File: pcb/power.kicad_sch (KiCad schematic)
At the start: 29 parts

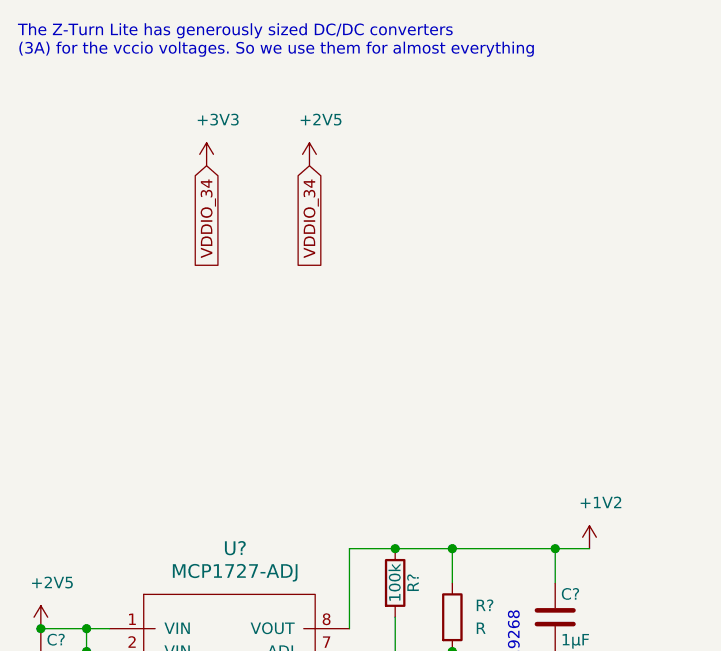
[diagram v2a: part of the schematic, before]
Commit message: add i2c addresses
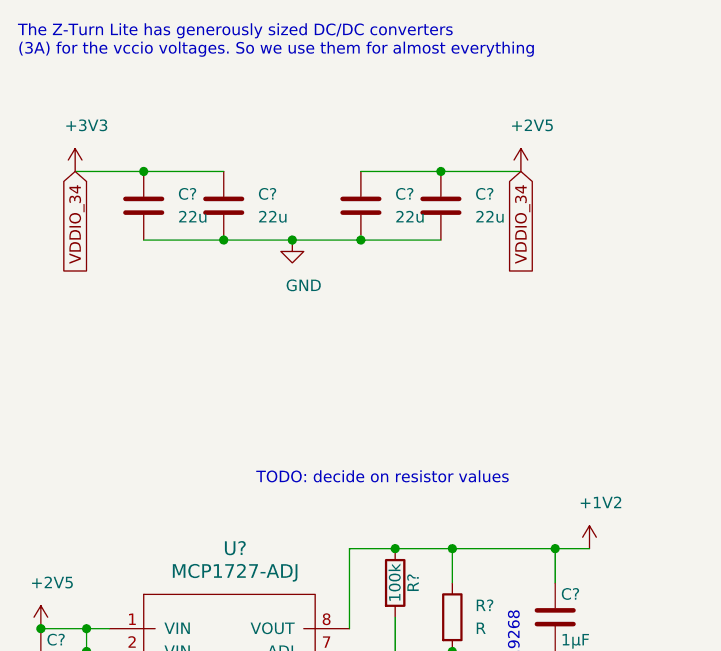
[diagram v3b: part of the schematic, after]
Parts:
- added C? (x4): 22u, symbol Device:C
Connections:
- net +2V5: now also C?.1, C?.1, C?.1, C?.1
- net GND: now also C?.2, C?.2, C?.2, C?.2
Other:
- note added: "TODO: decide on resistor values"
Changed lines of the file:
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@@
   (junction (at 36.83 163.83) (diameter 1.016) (color 0 0 0 0))
   (junction (at 36.83 166.37) (diameter 1.016) (color 0 0 0 0))
+  (junction (at 43.18 36.83) (diameter 1.016) (color 0 0 0 0))
+  (junction (at 52.07 44.45) (diameter 1.016) (color 0 0 0 0))
+  (junction (at 59.69 44.45) (diameter 1.016) (color 0 0 0 0))
+  (junction (at 67.31 44.45) (diameter 1.016) (color 0 0 0 0))
   (junction (at 71.12 78.74) (diameter 1.016) (color 0 0 0 0))
   (junction (at 71.12 115.57) (diameter 1.016) (color 0 0 0 0))
   (junction (at 71.12 154.94) (diameter 1.016) (color 0 0 0 0))
+  (junction (at 76.2 36.83) (diameter 1.016) (color 0 0 0 0))
   (junction (at 77.47 78.74) (diameter 1.016) (color 0 0 0 0))
   (junction (at 77.47 90.17) (diameter 1.016) (color 0 0 0 0))
@@
     (stroke (width 0) (type solid) (color 0 0 0 0))
   )
+  (wire (pts (xy 35.56 36.83) (xy 43.18 36.83))
+    (stroke (width 0) (type solid) (color 0 0 0 0))
+  )
   (wire (pts (xy 36.83 87.63) (xy 36.83 90.17))
     (stroke (width 0) (type solid) (color 0 0 0 0))
@@
     (stroke (width 0) (type solid) (color 0 0 0 0))
   )
+  (wire (pts (xy 43.18 36.83) (xy 52.07 36.83))
+    (stroke (width 0) (type solid) (color 0 0 0 0))
+  )
+  (wire (pts (xy 43.18 44.45) (xy 52.07 44.45))
+    (stroke (width 0) (type solid) (color 0 0 0 0))
+  )
+  (wire (pts (xy 52.07 44.45) (xy 59.69 44.45))
+    (stroke (width 0) (type solid) (color 0 0 0 0))
+  )
+  (wire (pts (xy 59.69 44.45) (xy 67.31 44.45))
+    (stroke (width 0) (type solid) (color 0 0 0 0))
+  )
   (wire (pts (xy 66.04 78.74) (xy 66.04 87.63))
     (stroke (width 0) (type solid) (color 0 0 0 0))
@@
     (stroke (width 0) (type solid) (color 0 0 0 0))
   )
+  (wire (pts (xy 67.31 36.83) (xy 76.2 36.83))
+    (stroke (width 0) (type solid) (color 0 0 0 0))
+  )
+  (wire (pts (xy 67.31 44.45) (xy 76.2 44.45))
+    (stroke (width 0) (type solid) (color 0 0 0 0))
+  )
   (wire (pts (xy 71.12 95.25) (xy 71.12 86.36))
     (stroke (width 0) (type solid) (color 0 0 0 0))
@@
   )
   (wire (pts (xy 71.12 171.45) (xy 71.12 162.56))
+    (stroke (width 0) (type solid) (color 0 0 0 0))
+  )
+  (wire (pts (xy 76.2 36.83) (xy 85.09 36.83))
     (stroke (width 0) (type solid) (color 0 0 0 0))
   )
@@
     (effects (font (size 1.27 1.27)) (justify left bottom))
   )
+  (text "TODO: decide on resistor values" (at 83.82 71.755 180)
+    (effects (font (size 1.27 1.27)) (justify right bottom))
+  )
   (text "1: 1.9268" (at 85.09 85.725 270)
     (effects (font (size 1.27 1.27)) (justify right bottom))
@@
     (effects (font (size 1.27 1.27)) (justify right bottom))
   )
-  (global_label "VDDIO_34" (shape input) (at 50.165 36.195 270)    (property "Intersheet References" "${INTERSHEET_REFS}" (id 0) (at 50.0856 49.0826 90)
+  (global_label "VDDIO_34" (shape input) (at 35.56 36.83 270)    (property "Intersheet References" "${INTERSHEET_REFS}" (id 0) (at 35.4806 49.7176 90)
       (effects (font (size 1.27 1.27)) (justify right) hide)
     )
     (effects (font (size 1.27 1.27)) (justify right))
   )
-  (global_label "VDDIO_34" (shape input) (at 61.595 36.195 270)    (property "Intersheet References" "${INTERSHEET_REFS}" (id 0) (at 61.5156 49.0826 90)
+  (global_label "VDDIO_34" (shape input) (at 85.09 36.83 270)    (property "Intersheet References" "${INTERSHEET_REFS}" (id 0) (at 85.0106 49.7176 90)
       (effects (font (size 1.27 1.27)) (justify right) hide)
     )
@@
     )
   )
-  (symbol (lib_id "power:+3V3") (at 50.165 36.195 0) (unit 1)
-    (in_bom yes) (on_board yes)
-    (property "Reference" "#PWR?" (id 0) (at 50.165 40.005 0)
-      (effects (font (size 1.27 1.27)) hide)
-    )
-    (property "Value" "+3V3" (id 1) (at 51.435 31.115 0))
-    (property "Footprint" "" (id 2) (at 50.165 36.195 0)
-      (effects (font (size 1.27 1.27)) hide)
-    )
-    (property "Datasheet" "" (id 3) (at 50.165 36.195 0)
-      (effects (font (size 1.27 1.27)) hide)
-    )
-  )
-  (symbol (lib_id "power:+2V5") (at 61.595 36.195 0) (unit 1)
-    (in_bom yes) (on_board yes)
-    (property "Reference" "#PWR?" (id 0) (at 61.595 40.005 0)
-      (effects (font (size 1.27 1.27)) hide)
-    )
-    (property "Value" "+2V5" (id 1) (at 62.865 31.115 0))
-    (property "Footprint" "" (id 2) (at 61.595 36.195 0)
-      (effects (font (size 1.27 1.27)) hide)
-    )
-    (property "Datasheet" "" (id 3) (at 61.595 36.195 0)
+  (symbol (lib_id "power:+3V3") (at 35.56 36.83 0) (unit 1)
+    (in_bom yes) (on_board yes)
+    (property "Reference" "#PWR?" (id 0) (at 35.56 40.64 0)
+      (effects (font (size 1.27 1.27)) hide)
+    )
+    (property "Value" "+3V3" (id 1) (at 36.83 31.75 0))
+    (property "Footprint" "" (id 2) (at 35.56 36.83 0)
+      (effects (font (size 1.27 1.27)) hide)
+    )
+    (property "Datasheet" "" (id 3) (at 35.56 36.83 0)
+      (effects (font (size 1.27 1.27)) hide)
+    )
+  )
+  (symbol (lib_id "power:+2V5") (at 85.09 36.83 0) (unit 1)
+    (in_bom yes) (on_board yes)
+    (property "Reference" "#PWR?" (id 0) (at 85.09 40.64 0)
+      (effects (font (size 1.27 1.27)) hide)
+    )
+    (property "Value" "+2V5" (id 1) (at 86.36 31.75 0))
+    (property "Footprint" "" (id 2) (at 85.09 36.83 0)
+      (effects (font (size 1.27 1.27)) hide)
+    )
+    (property "Datasheet" "" (id 3) (at 85.09 36.83 0)
       (effects (font (size 1.27 1.27)) hide)
     )
@@
     )
     (property "Datasheet" "" (id 3) (at 31.75 171.45 0)
+      (effects (font (size 1.27 1.27)) hide)
+    )
+  )
+  (symbol (lib_id "power:GND") (at 59.69 44.45 0) (unit 1)
+    (in_bom yes) (on_board yes)
+    (property "Reference" "#PWR?" (id 0) (at 59.69 50.8 0)
+      (effects (font (size 1.27 1.27)) hide)
+    )
+    (property "Value" "GND" (id 1) (at 60.96 49.53 0))
+    (property "Footprint" "" (id 2) (at 59.69 44.45 0)
+      (effects (font (size 1.27 1.27)) hide)
+    )
+    (property "Datasheet" "" (id 3) (at 59.69 44.45 0)
       (effects (font (size 1.27 1.27)) hide)
     )
@@
       (effects (font (size 1.27 1.27)) hide)
     )
+  )
+  (symbol (lib_id "Device:C") (at 43.18 40.64 0) (unit 1)
+    (in_bom yes) (on_board yes)
+    (property "Reference" "C?" (id 0) (at 46.99 39.37 0)
+      (effects (font (size 1.27 1.27)) (justify left))
+    )
+    (property "Value" "22u" (id 1) (at 46.99 41.91 0)
+      (effects (font (size 1.27 1.27)) (justify left))
+    )
+    (property "Footprint" "" (id 2) (at 44.1452 44.45 0)
+      (effects (font (size 1.27 1.27)) hide)
+    )
+    (property "Datasheet" "~" (id 3) (at 43.18 40.64 0)
+      (effects (font (size 1.27 1.27)) hide)
+    )
+  )
+  (symbol (lib_id "Device:C") (at 52.07 40.64 0) (unit 1)
+    (in_bom yes) (on_board yes)
+    (property "Reference" "C?" (id 0) (at 55.88 39.37 0)
+      (effects (font (size 1.27 1.27)) (justify left))
+    )
+    (property "Value" "22u" (id 1) (at 55.88 41.91 0)
+      (effects (font (size 1.27 1.27)) (justify left))
+    )
+    (property "Footprint" "" (id 2) (at 53.0352 44.45 0)
+      (effects (font (size 1.27 1.27)) hide)
+    )
+    (property "Datasheet" "~" (id 3) (at 52.07 40.64 0)
+      (effects (font (size 1.27 1.27)) hide)
+    )
+  )
+  (symbol (lib_id "Device:C") (at 67.31 40.64 0) (unit 1)
+    (in_bom yes) (on_board yes)
+    (property "Reference" "C?" (id 0) (at 71.12 39.37 0)
+      (effects (font (size 1.27 1.27)) (justify left))
+    )
+    (property "Value" "22u" (id 1) (at 71.12 41.91 0)
+      (effects (font (size 1.27 1.27)) (justify left))
+    )
+    (property "Footprint" "" (id 2) (at 68.2752 44.45 0)
+      (effects (font (size 1.27 1.27)) hide)
+    )
+    (property "Datasheet" "~" (id 3) (at 67.31 40.64 0)
+      (effects (font (size 1.27 1.27)) hide)
+    )
+  )
+  (symbol (lib_id "Device:C") (at 76.2 40.64 0) (unit 1)
+    (in_bom yes) (on_board yes)
+    (property "Reference" "C?" (id 0) (at 80.01 39.37 0)
+      (effects (font (size 1.27 1.27)) (justify left))
+    )
+    (property "Value" "22u" (id 1) (at 80.01 41.91 0)
+      (effects (font (size 1.27 1.27)) (justify left))
+    )
+    (property "Footprint" "" (id 2) (at 77.1652 44.45 0)
+      (effects (font (size 1.27 1.27)) hide)
+    )
+    (property "Datasheet" "~" (id 3) (at 76.2 40.64 0)
+      (effects (font (size 1.27 1.27)) hide)
+    )
